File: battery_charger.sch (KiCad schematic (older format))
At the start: 15 parts

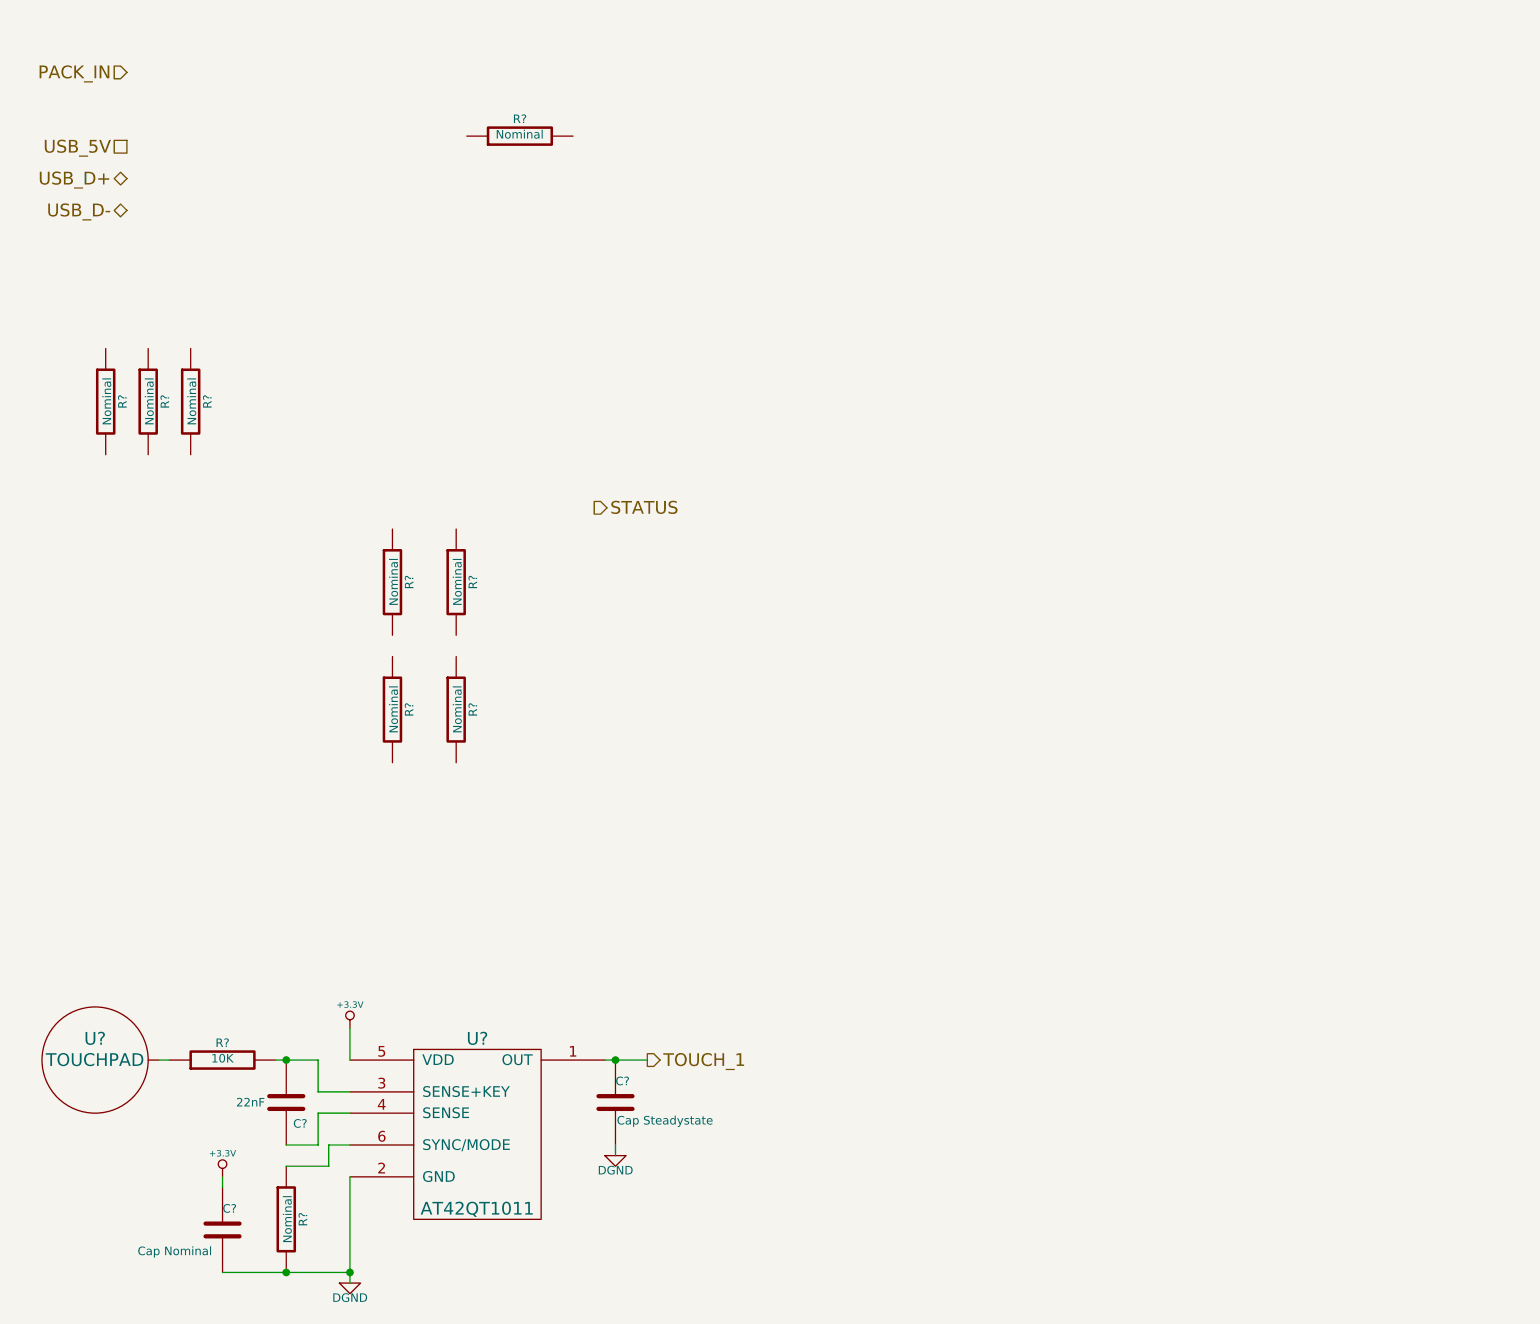
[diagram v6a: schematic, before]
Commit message: started working on charging IC
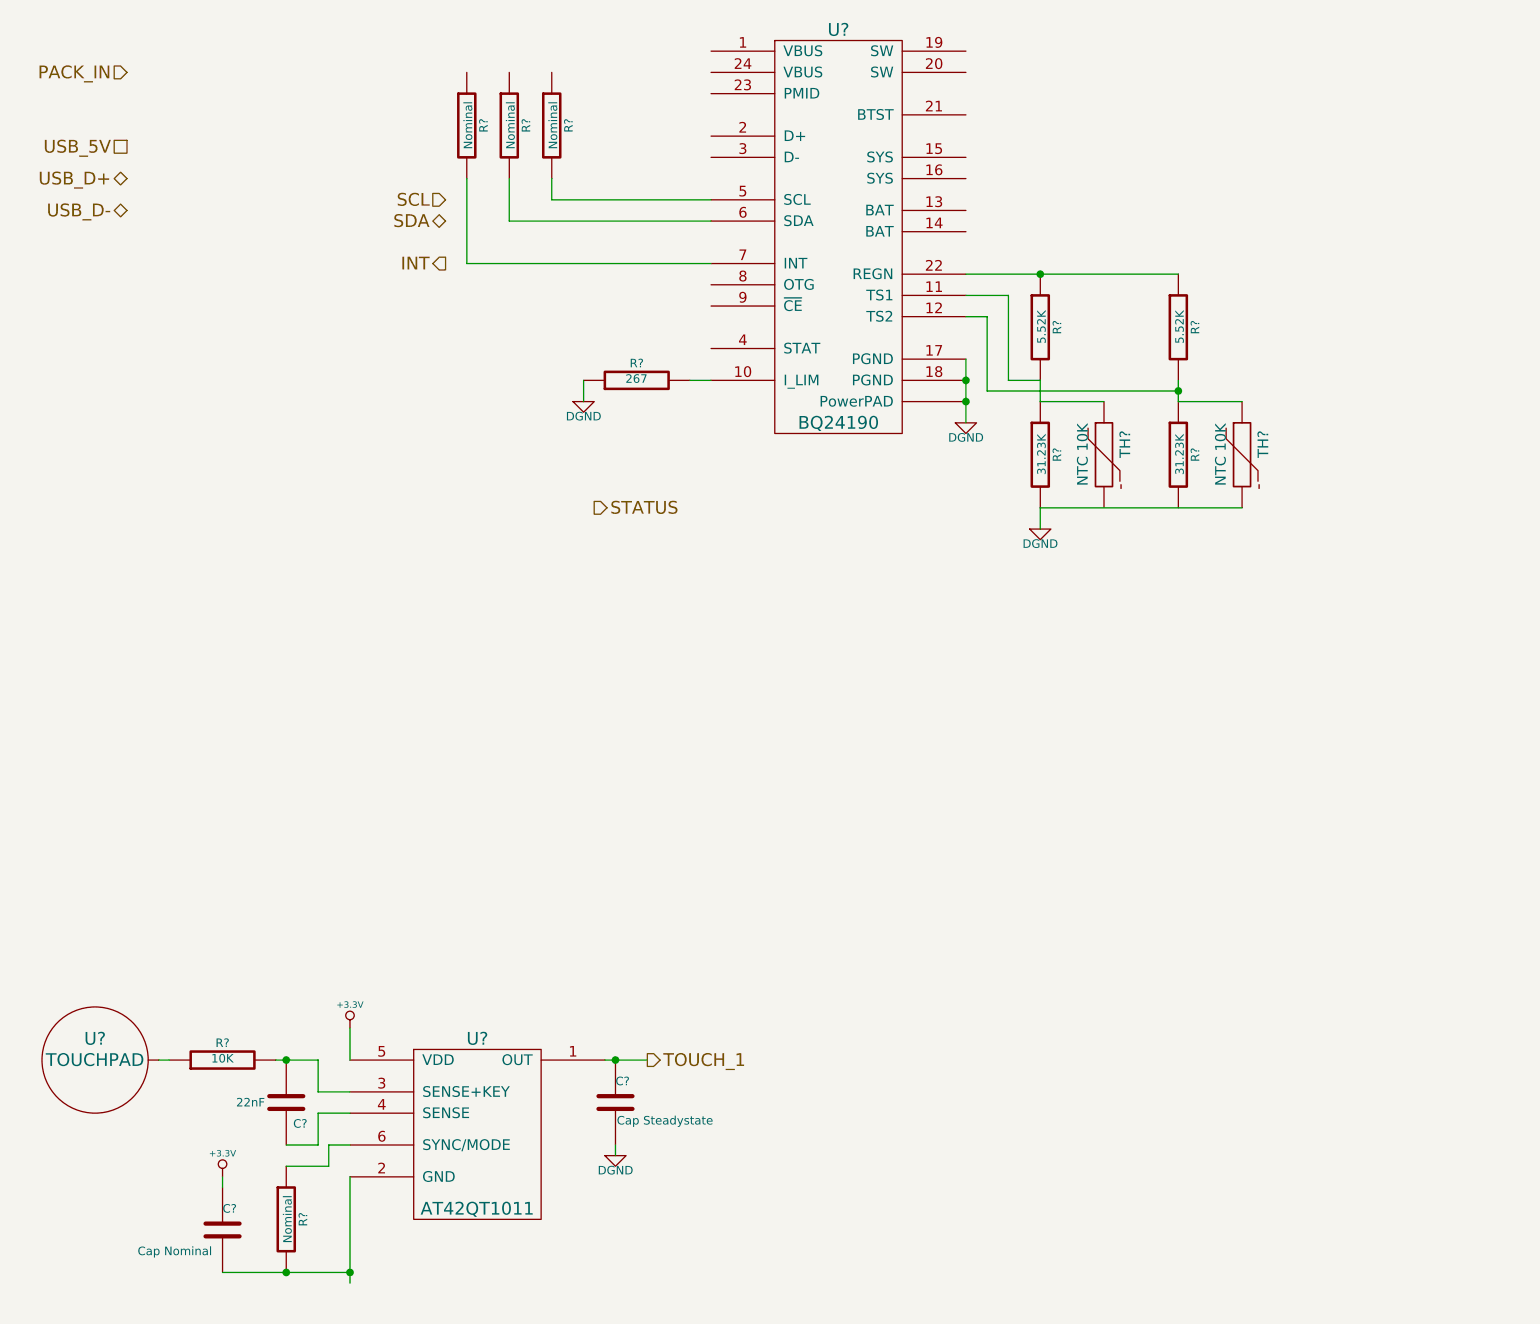
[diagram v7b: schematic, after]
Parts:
- added TH? (x2): NTC 10K, ~, symbol THERMISTOR
- added U?: BQ24190, ~, symbol BQ24190
- R? (x2): value Nominal -> 5.52K
- R? (x2): value Nominal -> 31.23K
- R?: value Nominal -> 267
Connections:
- net DGND: now also R?.1, R?.2, TH?.2, U?.17 (PGND), U?.18 (PGND), U?.~ (PowerPAD); no longer C?.2, R?.2, U?.2 (GND)
- net at R?.2: now also U?.7 (INT)
- net at R?.2: now also U?.6 (SDA)
- net at R?.2: now also U?.5 (SCL)
- net at R?.1: now also R?.1, U?.22 (REGN)
- net at R?.2: now also R?.1, TH?.1, U?.11 (TS1)
- net at R?.2: now also R?.1, TH?.1, U?.12 (TS2)
- net at R?.2: now also U?.10 (I_LIM)
- new net: C?.2, R?.2, U?.2 (GND)
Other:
- moved on the sheet: R?
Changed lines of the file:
@@
 Sheet 14 18
 Title ""
-Date "11 dec 2013"
+Date "12 dec 2013"
 Rev ""
 Comp ""
@@
 L DGND #PWR?
 U 1 1 5292B82E
-P 2500 6750
-F 0 "#PWR?" H 2500 6750 40  0001 C CNN
-F 1 "DGND" H 2500 6680 40  0000 C CNN
-F 2 "" H 2500 6750 60  0000 C CNN
-F 3 "" H 2500 6750 60  0000 C CNN
-	1    2500 6750
+P 3600 2600
+F 0 "#PWR?" H 3600 2600 40  0001 C CNN
+F 1 "DGND" H 3600 2530 40  0000 C CNN
+F 2 "" H 3600 2600 60  0000 C CNN
+F 3 "" H 3600 2600 60  0000 C CNN
+	1    3600 2600
 	1    0    0    -1
 $EndComp
@@
 	1    0    0    -1
 $EndComp
-Wire Wire Line
-	1650 5700 1600 5700
-Wire Wire Line
-	2150 5700 2200 5700
-Wire Wire Line
-	2200 5700 2350 5700
-Wire Wire Line
-	2350 5700 2350 5850
-Wire Wire Line
-	2350 5850 2500 5850
-Wire Wire Line
-	2200 6100 2350 6100
-Wire Wire Line
-	2350 6100 2350 5950
-Wire Wire Line
-	2350 5950 2500 5950
-Connection ~ 2200 5700
-Wire Wire Line
-	2500 5550 2500 5700
-Wire Wire Line
-	2500 6250 2500 6700
-Wire Wire Line
-	2500 6700 2500 6750
-Wire Wire Line
-	2400 6200 2400 6100
-Wire Wire Line
-	2400 6100 2500 6100
-Connection ~ 2500 6700
-Wire Wire Line
-	2400 6200 2200 6200
-Wire Wire Line
-	1900 6700 2200 6700
-Wire Wire Line
-	2200 6700 2500 6700
 $Comp
 L C C?
@@
 	1    0    0    -1
 $EndComp
-Wire Wire Line
-	1900 6250 1900 6300
-Connection ~ 2200 6700
 $Comp
 L C C?
@@
 	1    0    0    -1
 $EndComp
-Wire Wire Line
-	3700 5700 3750 5700
-Wire Wire Line
-	3750 5700 3900 5700
 $Comp
 L DGND #PWR?
@@
 	1    0    0    -1
 $EndComp
-Wire Wire Line
-	3750 6100 3750 6150
-Connection ~ 3750 5700
 Text HLabel 3900 5700 2    60   Output ~ 0
 TOUCH_1
@@
 L R R?
 U 1 1 5292B87D
-P 1350 2600
-F 0 "R?" V 1430 2600 40  0000 C CNN
-F 1 "Nominal" V 1357 2601 40  0000 C CNN
-F 2 "~" V 1280 2600 30  0000 C CNN
-F 3 "~" H 1350 2600 30  0000 C CNN
-	1    1350 2600
+P 3050 1300
+F 0 "R?" V 3130 1300 40  0000 C CNN
+F 1 "Nominal" V 3057 1301 40  0000 C CNN
+F 2 "~" V 2980 1300 30  0000 C CNN
+F 3 "~" H 3050 1300 30  0000 C CNN
+	1    3050 1300
 	1    0    0    -1
 $EndComp
@@
 L R R?
 U 1 1 5292B883
-P 1550 2600
-F 0 "R?" V 1630 2600 40  0000 C CNN
-F 1 "Nominal" V 1557 2601 40  0000 C CNN
-F 2 "~" V 1480 2600 30  0000 C CNN
-F 3 "~" H 1550 2600 30  0000 C CNN
-	1    1550 2600
+P 3250 1300
+F 0 "R?" V 3330 1300 40  0000 C CNN
+F 1 "Nominal" V 3257 1301 40  0000 C CNN
+F 2 "~" V 3180 1300 30  0000 C CNN
+F 3 "~" H 3250 1300 30  0000 C CNN
+	1    3250 1300
 	1    0    0    -1
 $EndComp
@@
 L R R?
 U 1 1 5292B889
-P 1750 2600
-F 0 "R?" V 1830 2600 40  0000 C CNN
-F 1 "Nominal" V 1757 2601 40  0000 C CNN
-F 2 "~" V 1680 2600 30  0000 C CNN
-F 3 "~" H 1750 2600 30  0000 C CNN
-	1    1750 2600
+P 3450 1300
+F 0 "R?" V 3530 1300 40  0000 C CNN
+F 1 "Nominal" V 3457 1301 40  0000 C CNN
+F 2 "~" V 3380 1300 30  0000 C CNN
+F 3 "~" H 3450 1300 30  0000 C CNN
+	1    3450 1300
 	1    0    0    -1
 $EndComp
@@
 L R R?
 U 1 1 5292B88F
-P 2700 3450
-F 0 "R?" V 2780 3450 40  0000 C CNN
-F 1 "Nominal" V 2707 3451 40  0000 C CNN
-F 2 "~" V 2630 3450 30  0000 C CNN
-F 3 "~" H 2700 3450 30  0000 C CNN
-	1    2700 3450
+P 5750 2250
+F 0 "R?" V 5830 2250 40  0000 C CNN
+F 1 "5.52K" V 5757 2251 40  0000 C CNN
+F 2 "~" V 5680 2250 30  0000 C CNN
+F 3 "~" H 5750 2250 30  0000 C CNN
+	1    5750 2250
 	1    0    0    -1
 $EndComp
@@
 L R R?
 U 1 1 5292B895
-P 2700 4050
-F 0 "R?" V 2780 4050 40  0000 C CNN
-F 1 "Nominal" V 2707 4051 40  0000 C CNN
-F 2 "~" V 2630 4050 30  0000 C CNN
-F 3 "~" H 2700 4050 30  0000 C CNN
-	1    2700 4050
+P 5750 2850
+F 0 "R?" V 5830 2850 40  0000 C CNN
+F 1 "31.23K" V 5757 2851 40  0000 C CNN
+F 2 "~" V 5680 2850 30  0000 C CNN
+F 3 "~" H 5750 2850 30  0000 C CNN
+	1    5750 2850
 	1    0    0    -1
 $EndComp
@@
 L R R?
 U 1 1 5292B89B
-P 3000 3450
-F 0 "R?" V 3080 3450 40  0000 C CNN
-F 1 "Nominal" V 3007 3451 40  0000 C CNN
-F 2 "~" V 2930 3450 30  0000 C CNN
-F 3 "~" H 3000 3450 30  0000 C CNN
-	1    3000 3450
+P 6400 2250
+F 0 "R?" V 6480 2250 40  0000 C CNN
+F 1 "5.52K" V 6407 2251 40  0000 C CNN
+F 2 "~" V 6330 2250 30  0000 C CNN
+F 3 "~" H 6400 2250 30  0000 C CNN
+	1    6400 2250
 	1    0    0    -1
 $EndComp
@@
 L R R?
 U 1 1 5292B8A1
-P 3000 4050
-F 0 "R?" V 3080 4050 40  0000 C CNN
-F 1 "Nominal" V 3007 4051 40  0000 C CNN
-F 2 "~" V 2930 4050 30  0000 C CNN
-F 3 "~" H 3000 4050 30  0000 C CNN
-	1    3000 4050
+P 6400 2850
+F 0 "R?" V 6480 2850 40  0000 C CNN
+F 1 "31.23K" V 6407 2851 40  0000 C CNN
+F 2 "~" V 6330 2850 30  0000 C CNN
+F 3 "~" H 6400 2850 30  0000 C CNN
+	1    6400 2850
 	1    0    0    -1
 $EndComp
@@
 L R R?
 U 1 1 5292B8A7
-P 3300 1350
-F 0 "R?" V 3380 1350 40  0000 C CNN
-F 1 "Nominal" V 3307 1351 40  0000 C CNN
-F 2 "~" V 3230 1350 30  0000 C CNN
-F 3 "~" H 3300 1350 30  0000 C CNN
-	1    3300 1350
+P 3850 2500
+F 0 "R?" V 3930 2500 40  0000 C CNN
+F 1 "267" V 3857 2501 40  0000 C CNN
+F 2 "~" V 3780 2500 30  0000 C CNN
+F 3 "~" H 3850 2500 30  0000 C CNN
+	1    3850 2500
 	0    -1   -1   0
 $EndComp
@@
 Text HLabel 1450 1050 0    60   Input ~ 0
 PACK_IN
+$Comp
+L THERMISTOR TH?
+U 1 1 52A9865D
+P 6050 2850
+F 0 "TH?" V 6150 2900 50  0000 C CNN
+F 1 "NTC 10K" V 5950 2850 50  0000 C CNN
+F 2 "~" H 6050 2850 60  0000 C CNN
+F 3 "~" H 6050 2850 60  0000 C CNN
+	1    6050 2850
+	1    0    0    -1
+$EndComp
+$Comp
+L THERMISTOR TH?
+U 1 1 52A9866A
+P 6700 2850
+F 0 "TH?" V 6800 2900 50  0000 C CNN
+F 1 "NTC 10K" V 6600 2850 50  0000 C CNN
+F 2 "~" H 6700 2850 60  0000 C CNN
+F 3 "~" H 6700 2850 60  0000 C CNN
+	1    6700 2850
+	1    0    0    -1
+$EndComp
+$Comp
+L BQ24190 U?
+U 1 1 52A98672
+P 4800 850
+F 0 "U?" H 4800 850 60  0000 C CNN
+F 1 "BQ24190" H 4800 -1000 60  0000 C CNN
+F 2 "~" H 4800 850 60  0000 C CNN
+F 3 "~" H 4800 850 60  0000 C CNN
+	1    4800 850
+	1    0    0    -1
+$EndComp
+$Comp
+L DGND #PWR?
+U 1 1 52A986BA
+P 5400 2700
+F 0 "#PWR?" H 5400 2700 40  0001 C CNN
+F 1 "DGND" H 5400 2630 40  0000 C CNN
+F 2 "" H 5400 2700 60  0000 C CNN
+F 3 "" H 5400 2700 60  0000 C CNN
+	1    5400 2700
+	1    0    0    -1
+$EndComp
+Wire Wire Line
+	1650 5700 1600 5700
+Wire Wire Line
+	2150 5700 2350 5700
+Wire Wire Line
+	2350 5700 2350 5850
+Wire Wire Line
+	2350 5850 2500 5850
+Wire Wire Line
+	2200 6100 2350 6100
+Wire Wire Line
+	2350 6100 2350 5950
+Wire Wire Line
+	2350 5950 2500 5950
+Connection ~ 2200 5700
+Wire Wire Line
+	2500 5550 2500 5700
+Wire Wire Line
+	2500 6250 2500 6750
+Wire Wire Line
+	2400 6200 2400 6100
+Wire Wire Line
+	2400 6100 2500 6100
+Connection ~ 2500 6700
+Wire Wire Line
+	2400 6200 2200 6200
+Wire Wire Line
+	1900 6700 2500 6700
+Wire Wire Line
+	1900 6250 1900 6300
+Connection ~ 2200 6700
+Wire Wire Line
+	3700 5700 3900 5700
+Wire Wire Line
+	3750 6100 3750 6150
+Connection ~ 3750 5700
+Wire Wire Line
+	5400 2400 5400 2700
+Connection ~ 5400 2500
+Connection ~ 5400 2600
+Wire Wire Line
+	4100 2500 4200 2500
+Wire Wire Line
+	3600 2500 3600 2600
+Wire Wire Line
+	5400 2000 6400 2000
+Connection ~ 5750 2000
+Wire Wire Line
+	5400 2200 5500 2200
+Wire Wire Line
+	5500 2200 5500 2550
+Wire Wire Line
+	5500 2550 6400 2550
+Wire Wire Line
+	5750 2600 5750 2500
+Wire Wire Line
+	6050 2600 5750 2600
+Wire Wire Line
+	5750 3100 6700 3100
+$Comp
+L DGND #PWR?
+U 1 1 52A98A95
+P 5750 3200
+F 0 "#PWR?" H 5750 3200 40  0001 C CNN
+F 1 "DGND" H 5750 3130 40  0000 C CNN
+F 2 "" H 5750 3200 60  0000 C CNN
+F 3 "" H 5750 3200 60  0000 C CNN
+	1    5750 3200
+	1    0    0    -1
+$EndComp
+Wire Wire Line
+	5750 3100 5750 3200
+Wire Wire Line
+	5400 2100 5600 2100
+Wire Wire Line
+	5600 2100 5600 2500
+Wire Wire Line
+	5600 2500 5750 2500
+Wire Wire Line
+	6400 2500 6400 2600
+Connection ~ 6400 2550
+Wire Wire Line
+	6400 2600 6700 2600
+Wire Wire Line
+	3450 1550 3450 1650
+Wire Wire Line
+	3450 1650 4200 1650
+Wire Wire Line
+	4200 1750 3250 1750
+Wire Wire Line
+	3250 1750 3250 1550
+Wire Wire Line
+	3050 1550 3050 1950
+Wire Wire Line
+	3050 1950 4200 1950
+Text HLabel 2950 1650 0    60   Input ~ 0
+SCL
+Text HLabel 2950 1750 0    60   BiDi ~ 0
+SDA
+Text HLabel 2950 1950 0    60   Output ~ 0
+INT
 $EndSCHEMATC

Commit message: uh. same as before? some glitch
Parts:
- added C?: 1uF, ~, symbol C
- added C?: 6.8uF, ~, symbol C
- added C? (x3): 10uF, ~, symbol C
- added C?: 47nF, ~, symbol C
- added C?: 4.7uF, ~, symbol C
- added L?: 2.2uH, ~, symbol INDUCTOR
- added R?: Nominal, ~, symbol R
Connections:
- net +3.3V: now also R?.1, R?.1, R?.1, R?.1
- net DGND: now also C?.2, C?.2, C?.2, C?.2, C?.2, C?.2
- net INT: now also R?.2, U?.7 (INT)
- net SCL: now also R?.2, U?.5 (SCL)
- net SDA: now also R?.2, U?.6 (SDA)
- net STATUS: now also U?.4 (STAT), R?.2
- net USB_5V: now also U?.1 (VBUS), U?.24 (VBUS), C?.1
- net USB_D+: now also U?.2 (D+)
- net USB_D-: now also U?.3 (D-)
- net at R?.1, R?.1, U?.22 (REGN): now also C?.1
- net BATT: now reaches U?.13 (BAT)
- net BATT: now also U?.14 (BAT), C?.1
- net SYS_OUT: now reaches U?.15 (SYS)
- net SYS_OUT: now also U?.16 (SYS), C?.1, C?.1, L?.2
- net at U?.19 (SW): now also U?.20 (SW), C?.1, L?.1
- net at U?.21 (BTST): now also C?.2
- net at U?.23 (PMID): now also C?.1
- net OTG_EN: now reaches U?.8 (OTG)
- net ~CHG_EN: now reaches U?.9 (~CE)
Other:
- note added: "4A @ 3.65V Charging"
- note added: "Charger limited to 2A @ 5V"
- note added: "I_RIPPLE = 5*.5*.5/1.5/2.2 = 0.378A"
- note added: "I_SAT >= 4A + 0.5*I_RIPPLE = 4 + .5*.378 = 4.189A"
- note added: "X7R or X5R, 25V+\n2A+"
- note added: "X7R or X5R, 6V+\n109mA+"
- moved on the sheet: R?, TH?, U?
